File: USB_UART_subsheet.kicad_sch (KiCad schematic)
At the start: 13 parts, among them U2 FT232RL

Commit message: layout more
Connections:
- net 3V3OUT is gone; now on net VCCIO: C1.1, U2.17 (3V3OUT), U2.4 (VCCIO)
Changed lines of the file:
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@@
 		)
 	)
-	(label "3V3OUT"
+	(label "VCCIO"
 		(at 116.84 87.63 0)
 		(fields_autoplaced yes)

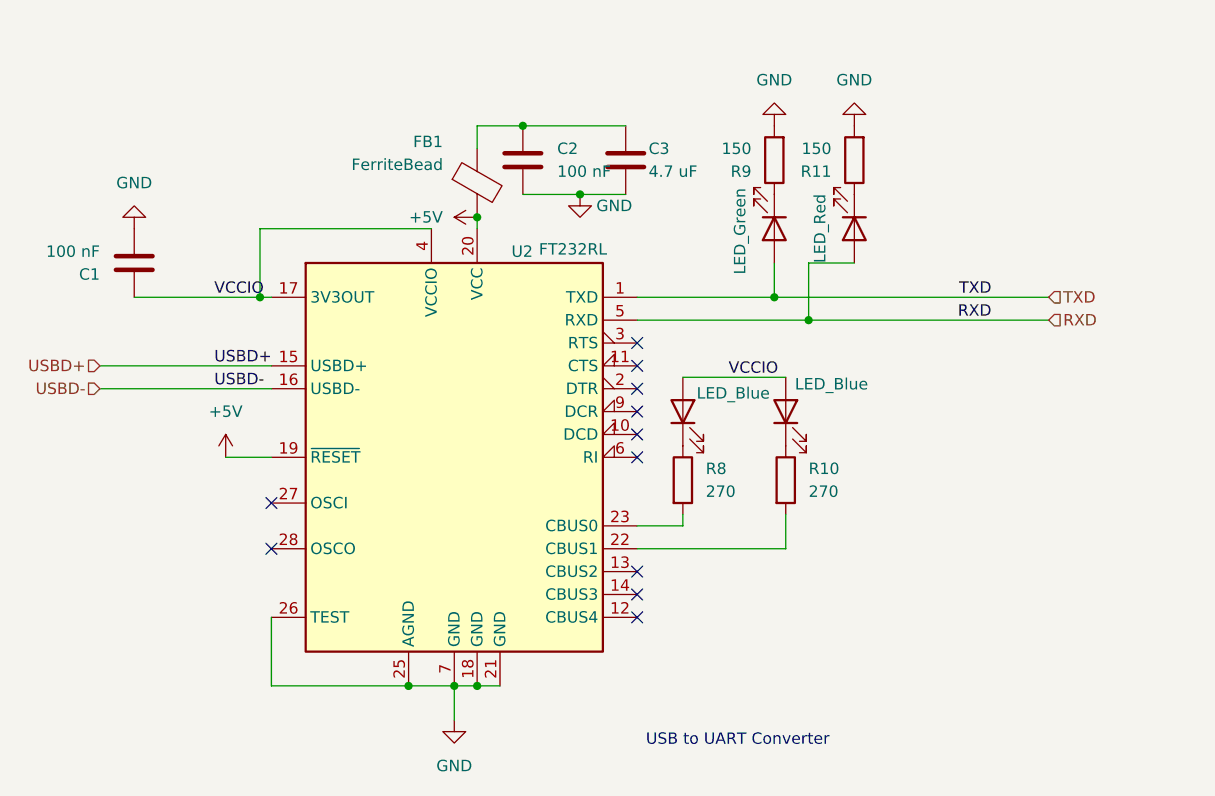
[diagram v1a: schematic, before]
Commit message: added testpoints to schematic for important sigs
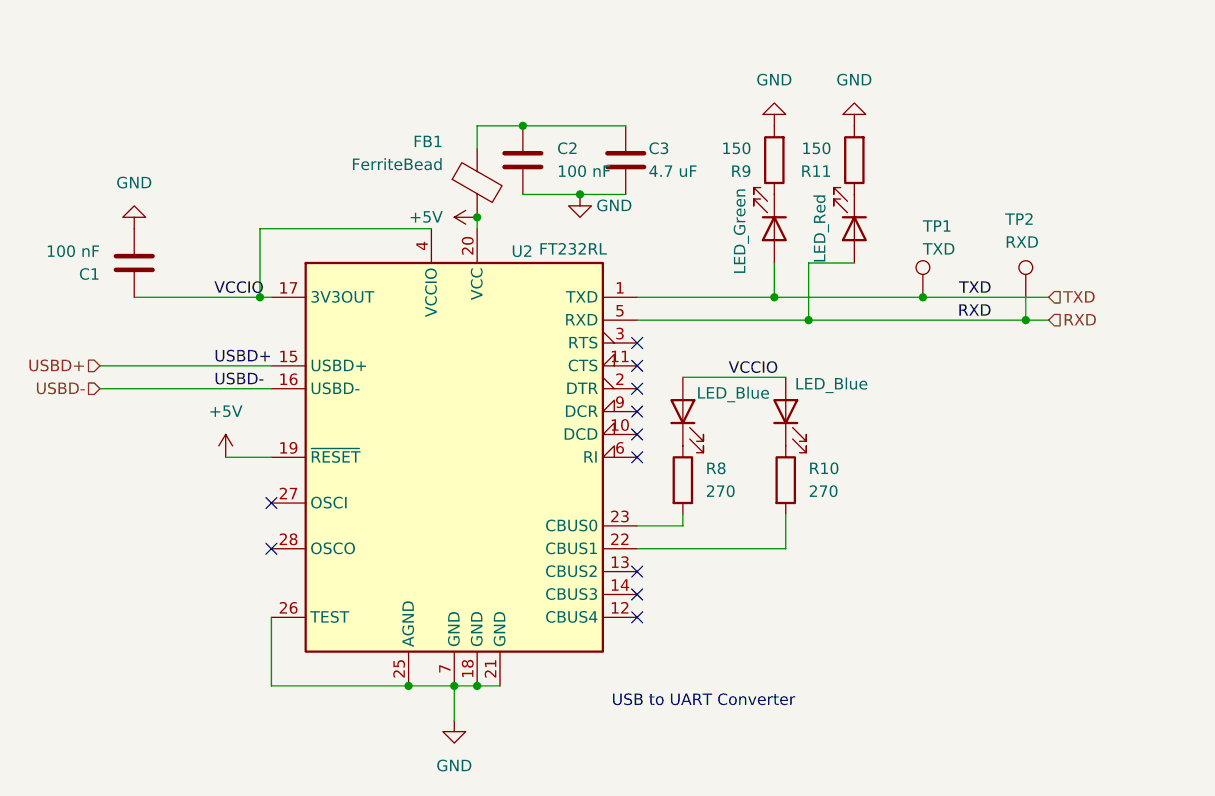
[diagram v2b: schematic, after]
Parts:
- added TP1: TXD, symbol Connector:TestPoint
- added TP2: RXD, symbol Connector:TestPoint
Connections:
- net RXD: now also TP2.1
- net TXD: now also TP1.1
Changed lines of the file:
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@@
+	)
+	(junction
+		(at 207.01 90.17)
+		(diameter 0)
+		(color 0 0 0 0)
 	)
 	(junction
@@
 	)
 	(junction
+		(at 195.58 87.63)
+		(diameter 0)
+		(color 0 0 0 0)
+	)
+	(junction
 		(at 143.51 130.81)
 		(diameter 0)
@@
 	(wire
 		(pts
-			(xy 182.88 90.17) (xy 209.55 90.17)
+			(xy 182.88 90.17) (xy 207.01 90.17)
 		)
 		(stroke
@@
 	(wire
 		(pts
-			(xy 179.07 87.63) (xy 209.55 87.63)
+			(xy 195.58 87.63) (xy 209.55 87.63)
+		)
+		(stroke
+			(width 0)
+			(type default)
+		)
+	)
+	(wire
+		(pts
+			(xy 179.07 87.63) (xy 195.58 87.63)
+		)
+		(stroke
+			(width 0)
+			(type default)
+		)
+	)
+	(wire
+		(pts
+			(xy 207.01 87.63) (xy 207.01 90.17)
 		)
 		(stroke
@@
 		(pts
 			(xy 104.14 95.25) (xy 123.19 95.25)
+		)
+		(stroke
+			(width 0)
+			(type default)
+		)
+	)
+	(wire
+		(pts
+			(xy 207.01 90.17) (xy 209.55 90.17)
 		)
 		(stroke
@@
 	(text "USB to UART Converter"
 		(exclude_from_sim no)
-		(at 175.006 136.906 0)
+		(at 171.196 132.588 0)
 		(effects
 			(font
@@
 				(path "/a0c17764-e0d1-4df5-b871-1489cf266494/8edd1d5f-65c6-4da1-89c4-ae03b62a6366"
 					(reference "R8")
+					(unit 1)
+				)
+			)
+		)
+	)
+	(symbol
+		(lib_id "Connector:TestPoint")
+		(at 207.01 87.63 0)
+		(unit 1)
+		(exclude_from_sim no)
+		(in_bom yes)
+		(on_board yes)
+		(dnp no)
+		(property "Reference" "TP2"
+			(at 204.724 78.994 0)
+			(effects
+				(font
+					(size 1.27 1.27)
+				)
+				(justify left)
+			)
+		)
+		(property "Value" "RXD"
+			(at 204.724 81.534 0)
+			(effects
+				(font
+					(size 1.27 1.27)
+				)
+				(justify left)
+			)
+		)
+		(property "Footprint" ""
+			(at 212.09 87.63 0)
+			(effects
+				(font
+					(size 1.27 1.27)
+				)
+				(hide yes)
+			)
+		)
+		(property "Datasheet" "~"
+			(at 212.09 87.63 0)
+			(effects
+				(font
+					(size 1.27 1.27)
+				)
+				(hide yes)
+			)
+		)
+		(property "Description" "test point"
+			(at 207.01 87.63 0)
+			(effects
+				(font
+					(size 1.27 1.27)
+				)
+				(hide yes)
+			)
+		)
+		(pin "1"
+		)
+		(instances
+			(project ""
+				(path "/a0c17764-e0d1-4df5-b871-1489cf266494/8edd1d5f-65c6-4da1-89c4-ae03b62a6366"
+					(reference "TP2")
 					(unit 1)
 				)
@@
 					(unit 1)
 				)
+			)
+		)
+	)
+	(symbol
+		(lib_id "Connector:TestPoint")
+		(at 195.58 87.63 0)
+		(unit 1)
+		(exclude_from_sim no)
+		(in_bom yes)
+		(on_board yes)
+		(dnp no)
+		(property "Reference" "TP1"
+			(at 195.58 79.756 0)
+			(effects
+				(font
+					(size 1.27 1.27)
+				)
+				(justify left)
+			)
+		)
+		(property "Value" "TXD"
+			(at 195.58 82.296 0)
+			(effects
+				(font
+					(size 1.27 1.27)
+				)
+				(justify left)
+			)
+		)
+		(property "Footprint" ""
+			(at 200.66 87.63 0)
+			(effects
+				(font
+					(size 1.27 1.27)
+				)
+				(hide yes)
+			)
+		)
+		(property "Datasheet" "~"
+			(at 200.66 87.63 0)
+			(effects
+				(font
+					(size 1.27 1.27)
+				)
+				(hide yes)
+			)
+		)
+		(property "Description" "test point"
+			(at 195.58 87.63 0)
+			(effects
+				(font
+					(size 1.27 1.27)
+				)
+				(hide yes)
+			)
+		)
+		(pin "1"
+		)
+		(instances
+			(project ""
+				(path "/a0c17764-e0d1-4df5-b871-1489cf266494/8edd1d5f-65c6-4da1-89c4-ae03b62a6366"
+					(reference "TP1")
+					(unit 1)
+				)

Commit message: going to set up for review
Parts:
- FB1: footprint Inductor_SMD:L_0201_0603Metric_Pad0.64x0.40mm_HandSolder -> Library:FB
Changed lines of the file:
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@@
 			)
 		)
-		(property "Footprint" "Inductor_SMD:L_0201_0603Metric_Pad0.64x0.40mm_HandSolder"
+		(property "Footprint" "Library:FB"
 			(at 144.272 74.93 90)
 			(effects

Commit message: more changes
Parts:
- removed D10: LED_Red, LED_SMD:LED_0805_2012Metric_Pad1.15x1.40mm_HandSolder, symbol Device:LED
- removed D8: LED_Green, LED_SMD:LED_0805_2012Metric_Pad1.15x1.40mm_HandSolder, symbol Device:LED
- removed R11, R9: 150, Resistor_SMD:R_0805_2012Metric_Pad1.20x1.40mm_HandSolder, symbol Device:R

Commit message: footprint
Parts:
- renumbered D9 to D8, R10 to R9
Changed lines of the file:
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@@
 		(on_board yes)
 		(dnp no)
-		(property "Reference" "D9"
+		(property "Reference" "D8"
 			(at 187.96 101.9175 0)
 			(effects
@@
 			(project "PCB_Schematic"
 				(path "/a0c17764-e0d1-4df5-b871-1489cf266494/8edd1d5f-65c6-4da1-89c4-ae03b62a6366"
-					(reference "D9")
+					(reference "D8")
 					(unit 1)
 				)
@@
 		(dnp no)
 		(fields_autoplaced yes)
-		(property "Reference" "R10"
+		(property "Reference" "R9"
 			(at 182.88 106.6799 0)
 			(effects
@@
 			(project "PCB_Schematic"
 				(path "/a0c17764-e0d1-4df5-b871-1489cf266494/8edd1d5f-65c6-4da1-89c4-ae03b62a6366"
-					(reference "R10")
-					(unit 1)
-				)
+					(reference "R9")
+					(unit 1)
+				)

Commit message: updates
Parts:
- removed TP1: TXD, symbol Connector:TestPoint
- removed TP2: RXD, symbol Connector:TestPoint
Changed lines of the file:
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@@
-	)
-	(junction
-		(at 207.01 90.17)
-		(diameter 0)
-		(color 0 0 0 0)
 	)
 	(junction
@@
 	)
 	(junction
-		(at 195.58 87.63)
-		(diameter 0)
-		(color 0 0 0 0)
-	)
-	(junction
 		(at 143.51 130.81)
 		(diameter 0)
@@
 	(wire
 		(pts
-			(xy 163.83 87.63) (xy 195.58 87.63)
+			(xy 163.83 87.63) (xy 209.55 87.63)
 		)
 		(stroke
@@
 	(wire
 		(pts
-			(xy 163.83 90.17) (xy 207.01 90.17)
+			(xy 163.83 90.17) (xy 209.55 90.17)
 		)
 		(stroke
@@
 	(wire
 		(pts
-			(xy 195.58 87.63) (xy 209.55 87.63)
-		)
-		(stroke
-			(width 0)
-			(type default)
-		)
-	)
-	(wire
-		(pts
-			(xy 207.01 87.63) (xy 207.01 90.17)
-		)
-		(stroke
-			(width 0)
-			(type default)
-		)
-	)
-	(wire
-		(pts
 			(xy 121.92 87.63) (xy 121.92 80.01)
 		)
@@
 		(pts
 			(xy 104.14 95.25) (xy 123.19 95.25)
-		)
-		(stroke
-			(width 0)
-			(type default)
-		)
-	)
-	(wire
-		(pts
-			(xy 207.01 90.17) (xy 209.55 90.17)
 		)
 		(stroke
@@
 				(path "/a0c17764-e0d1-4df5-b871-1489cf266494/8edd1d5f-65c6-4da1-89c4-ae03b62a6366"
 					(reference "R8")
-					(unit 1)
-				)
-			)
-		)
-	)
-	(symbol
-		(lib_id "Connector:TestPoint")
-		(at 207.01 87.63 0)
-		(unit 1)
-		(exclude_from_sim no)
-		(in_bom yes)
-		(on_board yes)
-		(dnp no)
-		(property "Reference" "TP2"
-			(at 204.724 78.994 0)
-			(effects
-				(font
-					(size 1.27 1.27)
-				)
-				(justify left)
-			)
-		)
-		(property "Value" "RXD"
-			(at 204.724 81.534 0)
-			(effects
-				(font
-					(size 1.27 1.27)
-				)
-				(justify left)
-			)
-		)
-		(property "Footprint" ""
-			(at 212.09 87.63 0)
-			(effects
-				(font
-					(size 1.27 1.27)
-				)
-				(hide yes)
-			)
-		)
-		(property "Datasheet" "~"
-			(at 212.09 87.63 0)
-			(effects
-				(font
-					(size 1.27 1.27)
-				)
-				(hide yes)
-			)
-		)
-		(property "Description" "test point"
-			(at 207.01 87.63 0)
-			(effects
-				(font
-					(size 1.27 1.27)
-				)
-				(hide yes)
-			)
-		)
-		(pin "1"
-		)
-		(instances
-			(project ""
-				(path "/a0c17764-e0d1-4df5-b871-1489cf266494/8edd1d5f-65c6-4da1-89c4-ae03b62a6366"
-					(reference "TP2")
 					(unit 1)
 				)
@@
 					(unit 1)
 				)
-			)
-		)
-	)
-	(symbol
-		(lib_id "Connector:TestPoint")
-		(at 195.58 87.63 0)
-		(unit 1)
-		(exclude_from_sim no)
-		(in_bom yes)
-		(on_board yes)
-		(dnp no)
-		(property "Reference" "TP1"
-			(at 195.58 79.756 0)
-			(effects
-				(font
-					(size 1.27 1.27)
-				)
-				(justify left)
-			)
-		)
-		(property "Value" "TXD"
-			(at 195.58 82.296 0)
-			(effects
-				(font
-					(size 1.27 1.27)
-				)
-				(justify left)
-			)
-		)
-		(property "Footprint" ""
-			(at 200.66 87.63 0)
-			(effects
-				(font
-					(size 1.27 1.27)
-				)
-				(hide yes)
-			)
-		)
-		(property "Datasheet" "~"
-			(at 200.66 87.63 0)
-			(effects
-				(font
-					(size 1.27 1.27)
-				)
-				(hide yes)
-			)
-		)
-		(property "Description" "test point"
-			(at 195.58 87.63 0)
-			(effects
-				(font
-					(size 1.27 1.27)
-				)
-				(hide yes)
-			)
-		)
-		(pin "1"
-		)
-		(instances
-			(project ""
-				(path "/a0c17764-e0d1-4df5-b871-1489cf266494/8edd1d5f-65c6-4da1-89c4-ae03b62a6366"
-					(reference "TP1")
-					(unit 1)
-				)

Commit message: finish touches
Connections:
- net +5V: now also C2.1, C3.1, FB1.1; no longer FB1.2, U2.20 (VCC)
- new net: FB1.2, U2.20 (VCC)
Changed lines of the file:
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@@
 	)
 	(junction
-		(at 146.05 78.74)
+		(at 151.13 68.58)
 		(diameter 0)
 		(color 0 0 0 0)
 	)
 	(junction
-		(at 151.13 68.58)
+		(at 146.05 68.58)
 		(diameter 0)
 		(color 0 0 0 0)
@@
 	)
 	(symbol
-		(lib_id "power:+5V")
-		(at 146.05 78.74 90)
-		(unit 1)
-		(exclude_from_sim no)
-		(in_bom yes)
-		(on_board yes)
-		(dnp no)
-		(fields_autoplaced yes)
-		(property "Reference" "#PWR015"
-			(at 149.86 78.74 0)
-			(effects
-				(font
-					(size 1.27 1.27)
-				)
-				(hide yes)
-			)
-		)
-		(property "Value" "+5V"
-			(at 142.24 78.7399 90)
-			(effects
-				(font
-					(size 1.27 1.27)
-				)
-				(justify left)
-			)
-		)
-		(property "Footprint" ""
-			(at 146.05 78.74 0)
-			(effects
-				(font
-					(size 1.27 1.27)
-				)
-				(hide yes)
-			)
-		)
-		(property "Datasheet" ""
-			(at 146.05 78.74 0)
-			(effects
-				(font
-					(size 1.27 1.27)
-				)
-				(hide yes)
-			)
-		)
-		(property "Description" "Power symbol creates a global label with name \"+5V\""
-			(at 146.05 78.74 0)
-			(effects
-				(font
-					(size 1.27 1.27)
-				)
-				(hide yes)
-			)
-		)
-		(pin "1"
-		)
-		(instances
-			(project "PCB_Schematic"
-				(path "/a0c17764-e0d1-4df5-b871-1489cf266494/8edd1d5f-65c6-4da1-89c4-ae03b62a6366"
-					(reference "#PWR015")
-					(unit 1)
-				)
-			)
-		)
-	)
-	(symbol
 		(lib_id "Interface_USB:FT232RL")
 		(at 143.51 105.41 0)
@@
 					(unit 1)
 				)
+			)
+		)
+	)
+	(symbol
+		(lib_id "power:+5V")
+		(at 146.05 68.58 0)
+		(unit 1)
+		(exclude_from_sim no)
+		(in_bom yes)
+		(on_board yes)
+		(dnp no)
+		(fields_autoplaced yes)
+		(property "Reference" "#PWR067"
+			(at 146.05 72.39 0)
+			(effects
+				(font
+					(size 1.27 1.27)
+				)
+				(hide yes)
+			)
+		)
+		(property "Value" "+5V"
+			(at 146.05 63.5 0)
+			(effects
+				(font
+					(size 1.27 1.27)
+				)
+			)
+		)
+		(property "Footprint" ""
+			(at 146.05 68.58 0)
+			(effects
+				(font
+					(size 1.27 1.27)
+				)
+				(hide yes)
+			)
+		)
+		(property "Datasheet" ""
+			(at 146.05 68.58 0)
+			(effects
+				(font
+					(size 1.27 1.27)
+				)
+				(hide yes)
+			)
+		)
+		(property "Description" "Power symbol creates a global label with name \"+5V\""
+			(at 146.05 68.58 0)
+			(effects
+				(font
+					(size 1.27 1.27)
+				)
+				(hide yes)
+			)
+		)
+		(pin "1"
+		)
+		(instances
+			(project ""
+				(path "/a0c17764-e0d1-4df5-b871-1489cf266494/8edd1d5f-65c6-4da1-89c4-ae03b62a6366"
+					(reference "#PWR067")
+					(unit 1)
+				)

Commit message: done
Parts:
- added R33: 10k, Resistor_SMD:R_0805_2012Metric_Pad1.20x1.40mm_HandSolder, symbol Device:R
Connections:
- net +5V: no longer C2.1, C3.1
- net CBUS0 : now reaches R8.2, U2.23 (CBUS0)
- net CBUS1: now reaches R9.2, U2.22 (CBUS1)
- net CTS: now reaches U2.11 (CTS)
- net CBUS4: now reaches U2.12 (CBUS4)
- net CBUS2: now reaches U2.13 (CBUS2)
- net CBUS3: now reaches U2.14 (CBUS3)
- net CBUS3: now also R33.1
- net Vcc: now reaches FB1.2, U2.20 (VCC)
- net Vcc: now also C2.1, C3.1, R33.2
- net RTS: now reaches U2.3 (RTS)
- no-connect marks 11 -> 10
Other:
- moved on the sheet: C2, C3, FB1
